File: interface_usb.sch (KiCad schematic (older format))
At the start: 0 parts

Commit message: Various components added
USB conn, general outputs, brake signal, touch sensor
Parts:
- added U?: CONN_USB, symbol CONN_USB
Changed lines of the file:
@@
 $Descr A4 11693 8268
 encoding utf-8
-Sheet 4 11
+Sheet 5 11
 Title ""
 Date "11 nov 2013"
@@
 Comment4 ""
 $EndDescr
+$Comp
+L CONN_USB U?
+U 1 1 52807223
+P 850 550
+F 0 "U?" H 850 550 60  0000 C CNN
+F 1 "CONN_USB" H 850 -100 60  0000 C CNN
+F 2 "" H 850 550 60  0000 C CNN
+F 3 "" H 850 550 60  0000 C CNN
+	1    850  550
+	1    0    0    -1
+$EndComp
 $EndSCHEMATC

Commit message: started fleshing out USB comm circuits
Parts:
- added C?: 22nF, ~, symbol C
- added C?: Cap Nominal, ~, symbol C
- added C?: Cap Steadystate, ~, symbol C
- added R?: 10K, ~, symbol R
- added R?: Nominal, ~, symbol R
- added U?: CP2110, symbol CP2110
- added U?: ESDR0502N, symbol ESDR0502N
- added U?: AT42QT1011, symbol AT42QT1011
- added U?: TOUCHPAD, symbol TOUCHPAD
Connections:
- net labels added: +3.3V, DGND, TOUCH_1
- wire segments 0 -> 34
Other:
- moved on the sheet: U?
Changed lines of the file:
@@
 Sheet 8 14
 Title ""
-Date "23 nov 2013"
+Date "24 nov 2013"
 Rev ""
 Comp ""
@@
 L CONN_USB U?
 U 1 1 52807223
-P 850 550
-F 0 "U?" H 850 550 60  0000 C CNN
-F 1 "CONN_USB" H 850 -100 60  0000 C CNN
-F 2 "" H 850 550 60  0000 C CNN
-F 3 "" H 850 550 60  0000 C CNN
-	1    850  550
-	1    0    0    -1
-$EndComp
+P 1650 2800
+F 0 "U?" H 1650 2800 60  0000 C CNN
+F 1 "CONN_USB" H 1650 2150 60  0000 C CNN
+F 2 "" H 1650 2800 60  0000 C CNN
+F 3 "" H 1650 2800 60  0000 C CNN
+	1    1650 2800
+	1    0    0    -1
+$EndComp
+$Comp
+L CP2110 U?
+U 1 1 5291A63B
+P 4250 2400
+F 0 "U?" H 4250 2400 60  0000 C CNN
+F 1 "CP2110" H 4250 700 60  0000 C CNN
+F 2 "" H 4250 2400 60  0000 C CNN
+F 3 "" H 4250 2400 60  0000 C CNN
+	1    4250 2400
+	1    0    0    -1
+$EndComp
+$Comp
+L ESDR0502N U?
+U 1 1 529256B4
+P 2700 2750
+F 0 "U?" H 2700 2750 60  0000 C CNN
+F 1 "ESDR0502N" H 2700 2050 60  0000 C CNN
+F 2 "" H 2700 2750 60  0000 C CNN
+F 3 "" H 2700 2750 60  0000 C CNN
+	1    2700 2750
+	1    0    0    -1
+$EndComp
+$Comp
+L AT42QT1011 U?
+U 1 1 52925A52
+P 3400 5700
+F 0 "U?" H 3400 5700 60  0000 C CNN
+F 1 "AT42QT1011" H 3400 4900 60  0000 C CNN
+F 2 "" H 3400 5700 60  0000 C CNN
+F 3 "" H 3400 5700 60  0000 C CNN
+	1    3400 5700
+	1    0    0    -1
+$EndComp
+$Comp
+L +3.3V #PWR?
+U 1 1 52925A58
+P 2450 4050
+F 0 "#PWR?" H 2450 4010 30  0001 C CNN
+F 1 "+3.3V" H 2450 4160 30  0000 C CNN
+F 2 "" H 2450 4050 60  0000 C CNN
+F 3 "" H 2450 4050 60  0000 C CNN
+	1    2450 4050
+	1    0    0    -1
+$EndComp
+$Comp
+L DGND #PWR?
+U 1 1 52925A5E
+P 2050 3400
+F 0 "#PWR?" H 2050 3400 40  0001 C CNN
+F 1 "DGND" H 2050 3330 40  0000 C CNN
+F 2 "" H 2050 3400 60  0000 C CNN
+F 3 "" H 2050 3400 60  0000 C CNN
+	1    2050 3400
+	1    0    0    -1
+$EndComp
+$Comp
+L R R?
+U 1 1 52925A64
+P 2200 5800
+F 0 "R?" V 2280 5800 40  0000 C CNN
+F 1 "10K" V 2207 5801 40  0000 C CNN
+F 2 "~" V 2130 5800 30  0000 C CNN
+F 3 "~" H 2200 5800 30  0000 C CNN
+	1    2200 5800
+	0    -1   -1   0
+$EndComp
+$Comp
+L C C?
+U 1 1 52925A6A
+P 2500 6000
+F 0 "C?" H 2400 6100 40  0000 L CNN
+F 1 "22nF" H 2600 6000 40  0000 L CNN
+F 2 "~" H 2538 5850 30  0000 C CNN
+F 3 "~" H 2500 6000 60  0000 C CNN
+	1    2500 6000
+	-1   0    0    1
+$EndComp
+$Comp
+L TOUCHPAD U?
+U 1 1 52925A70
+P 1600 5800
+F 0 "U?" H 1600 5900 60  0000 C CNN
+F 1 "TOUCHPAD" H 1600 5800 60  0000 C CNN
+F 2 "" H 1600 5800 60  0000 C CNN
+F 3 "" H 1600 5800 60  0000 C CNN
+	1    1600 5800
+	1    0    0    -1
+$EndComp
+$Comp
+L C C?
+U 1 1 52925A88
+P 2200 6600
+F 0 "C?" H 2200 6700 40  0000 L CNN
+F 1 "Cap Nominal" H 1800 6500 40  0000 L CNN
+F 2 "~" H 2238 6450 30  0000 C CNN
+F 3 "~" H 2200 6600 60  0000 C CNN
+	1    2200 6600
+	1    0    0    -1
+$EndComp
+$Comp
+L +3.3V #PWR?
+U 1 1 52925A8E
+P 2200 6350
+F 0 "#PWR?" H 2200 6310 30  0001 C CNN
+F 1 "+3.3V" H 2200 6460 30  0000 C CNN
+F 2 "" H 2200 6350 60  0000 C CNN
+F 3 "" H 2200 6350 60  0000 C CNN
+	1    2200 6350
+	1    0    0    -1
+$EndComp
+$Comp
+L C C?
+U 1 1 52925A96
+P 4050 6000
+F 0 "C?" H 4050 6100 40  0000 L CNN
+F 1 "Cap Steadystate" H 4056 5915 40  0000 L CNN
+F 2 "~" H 4088 5850 30  0000 C CNN
+F 3 "~" H 4050 6000 60  0000 C CNN
+	1    4050 6000
+	1    0    0    -1
+$EndComp
+$Comp
+L DGND #PWR?
+U 1 1 52925A9E
+P 4050 6250
+F 0 "#PWR?" H 4050 6250 40  0001 C CNN
+F 1 "DGND" H 4050 6180 40  0000 C CNN
+F 2 "" H 4050 6250 60  0000 C CNN
+F 3 "" H 4050 6250 60  0000 C CNN
+	1    4050 6250
+	1    0    0    -1
+$EndComp
+Text HLabel 4200 5800 2    60   Output ~ 0
+TOUCH_1
+$Comp
+L R R?
+U 1 1 52925AA7
+P 2500 6550
+F 0 "R?" V 2580 6550 40  0000 C CNN
+F 1 "Nominal" V 2507 6551 40  0000 C CNN
+F 2 "~" V 2430 6550 30  0000 C CNN
+F 3 "~" H 2500 6550 30  0000 C CNN
+	1    2500 6550
+	1    0    0    -1
+$EndComp
+Wire Wire Line
+	1950 5800 1900 5800
+Wire Wire Line
+	2450 5800 2500 5800
+Wire Wire Line
+	2500 5800 2650 5800
+Wire Wire Line
+	2650 5800 2650 5950
+Wire Wire Line
+	2650 5950 2800 5950
+Wire Wire Line
+	2500 6200 2650 6200
+Wire Wire Line
+	2650 6200 2650 6050
+Wire Wire Line
+	2650 6050 2800 6050
+Connection ~ 2500 5800
+Wire Wire Line
+	2800 5650 2800 5800
+Wire Wire Line
+	2800 6350 2800 6800
+Wire Wire Line
+	2800 6800 2800 6850
+Wire Wire Line
+	2700 6300 2700 6200
+Wire Wire Line
+	2700 6200 2800 6200
+Connection ~ 2800 6800
+Wire Wire Line
+	2700 6300 2500 6300
+Wire Wire Line
+	2200 6800 2500 6800
+Wire Wire Line
+	2500 6800 2800 6800
+Wire Wire Line
+	2200 6350 2200 6400
+Connection ~ 2500 6800
+Wire Wire Line
+	4000 5800 4050 5800
+Wire Wire Line
+	4050 5800 4200 5800
+Wire Wire Line
+	4050 6200 4050 6250
+Connection ~ 4050 5800
+Wire Wire Line
+	2300 3050 2300 2800
+Wire Wire Line
+	2300 2800 3100 2800
+Wire Wire Line
+	3100 2800 3100 3050
+Wire Wire Line
+	2300 3150 2300 3550
+Wire Wire Line
+	2300 3550 3100 3550
+Wire Wire Line
+	3100 3550 3100 3150
+Wire Wire Line
+	2000 2950 2100 2950
+Wire Wire Line
+	2000 3350 2050 3350
+Wire Wire Line
+	2050 3350 2100 3350
+Wire Wire Line
+	2050 3350 2050 3400
+Connection ~ 2050 3350
+Wire Wire Line
+	3100 3050 3400 3050
+Wire Wire Line
+	3100 3150 3400 3150
+Wire Wire Line
+	2000 3050 2300 3050
+Wire Wire Line
+	2000 3150 2300 3150
 $EndSCHEMATC

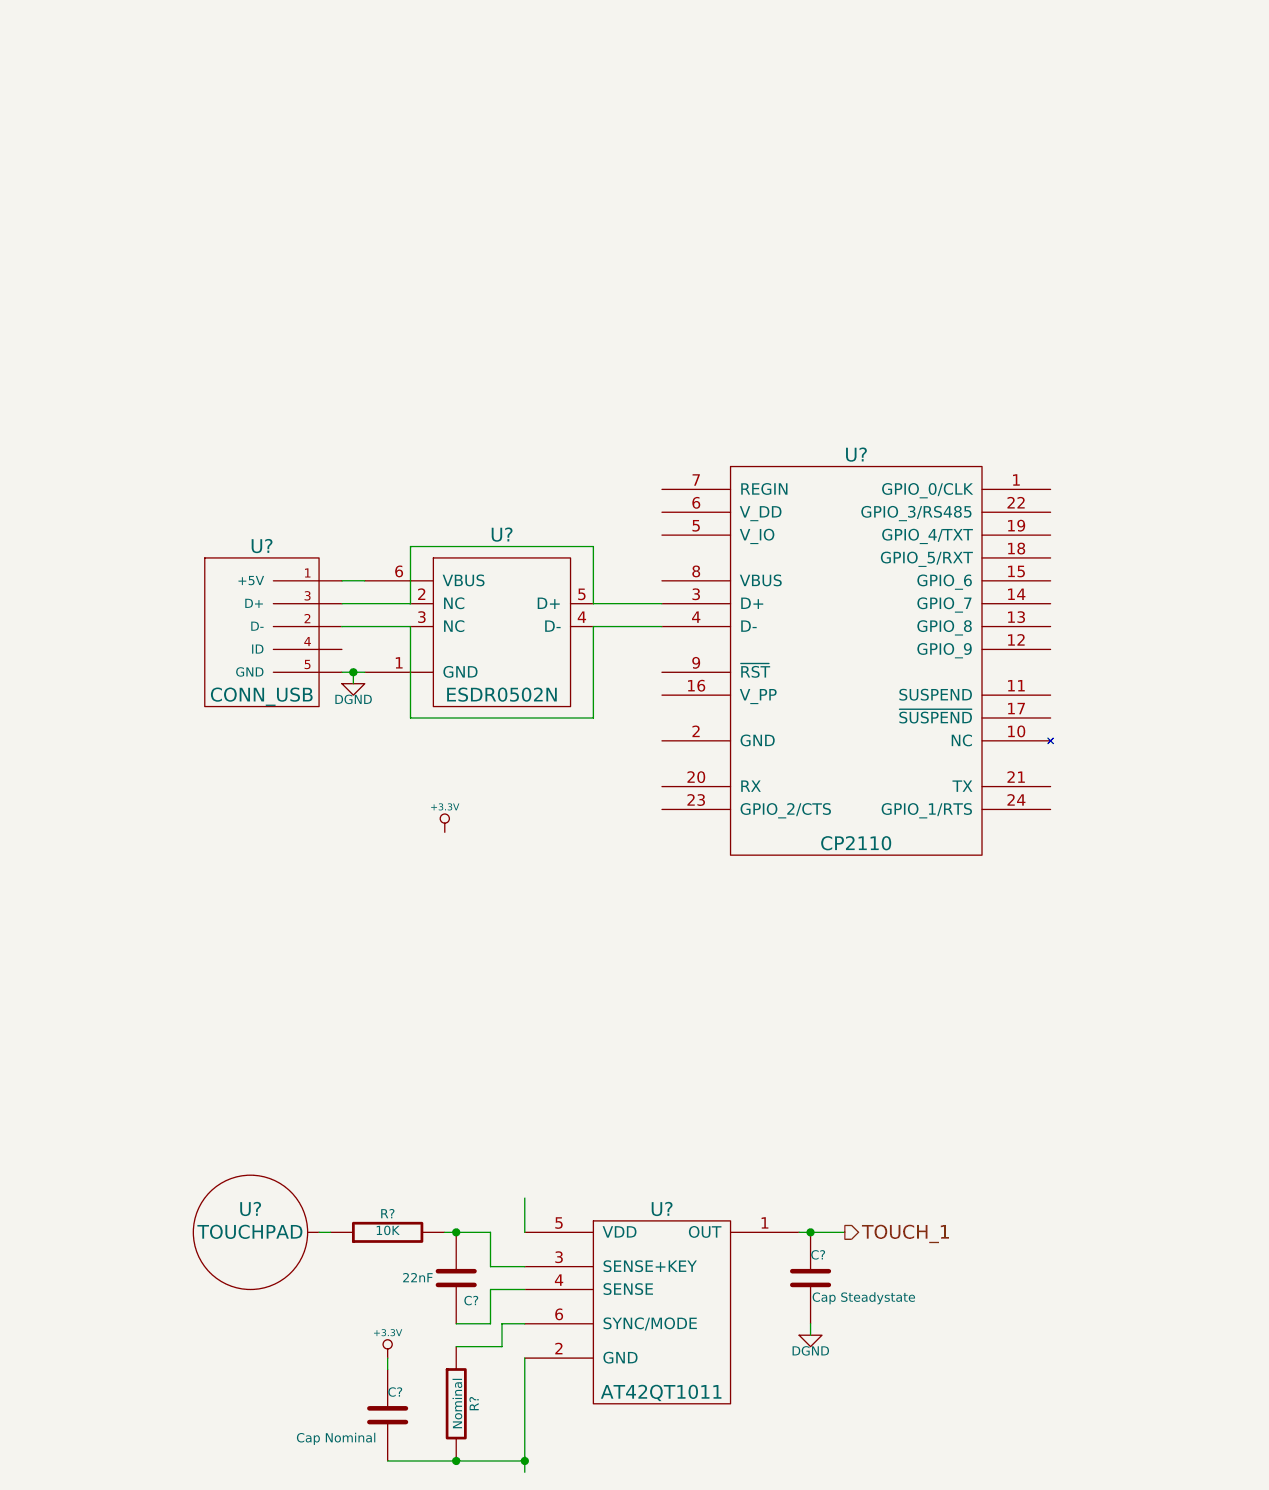
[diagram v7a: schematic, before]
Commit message: completed USB comm circuits
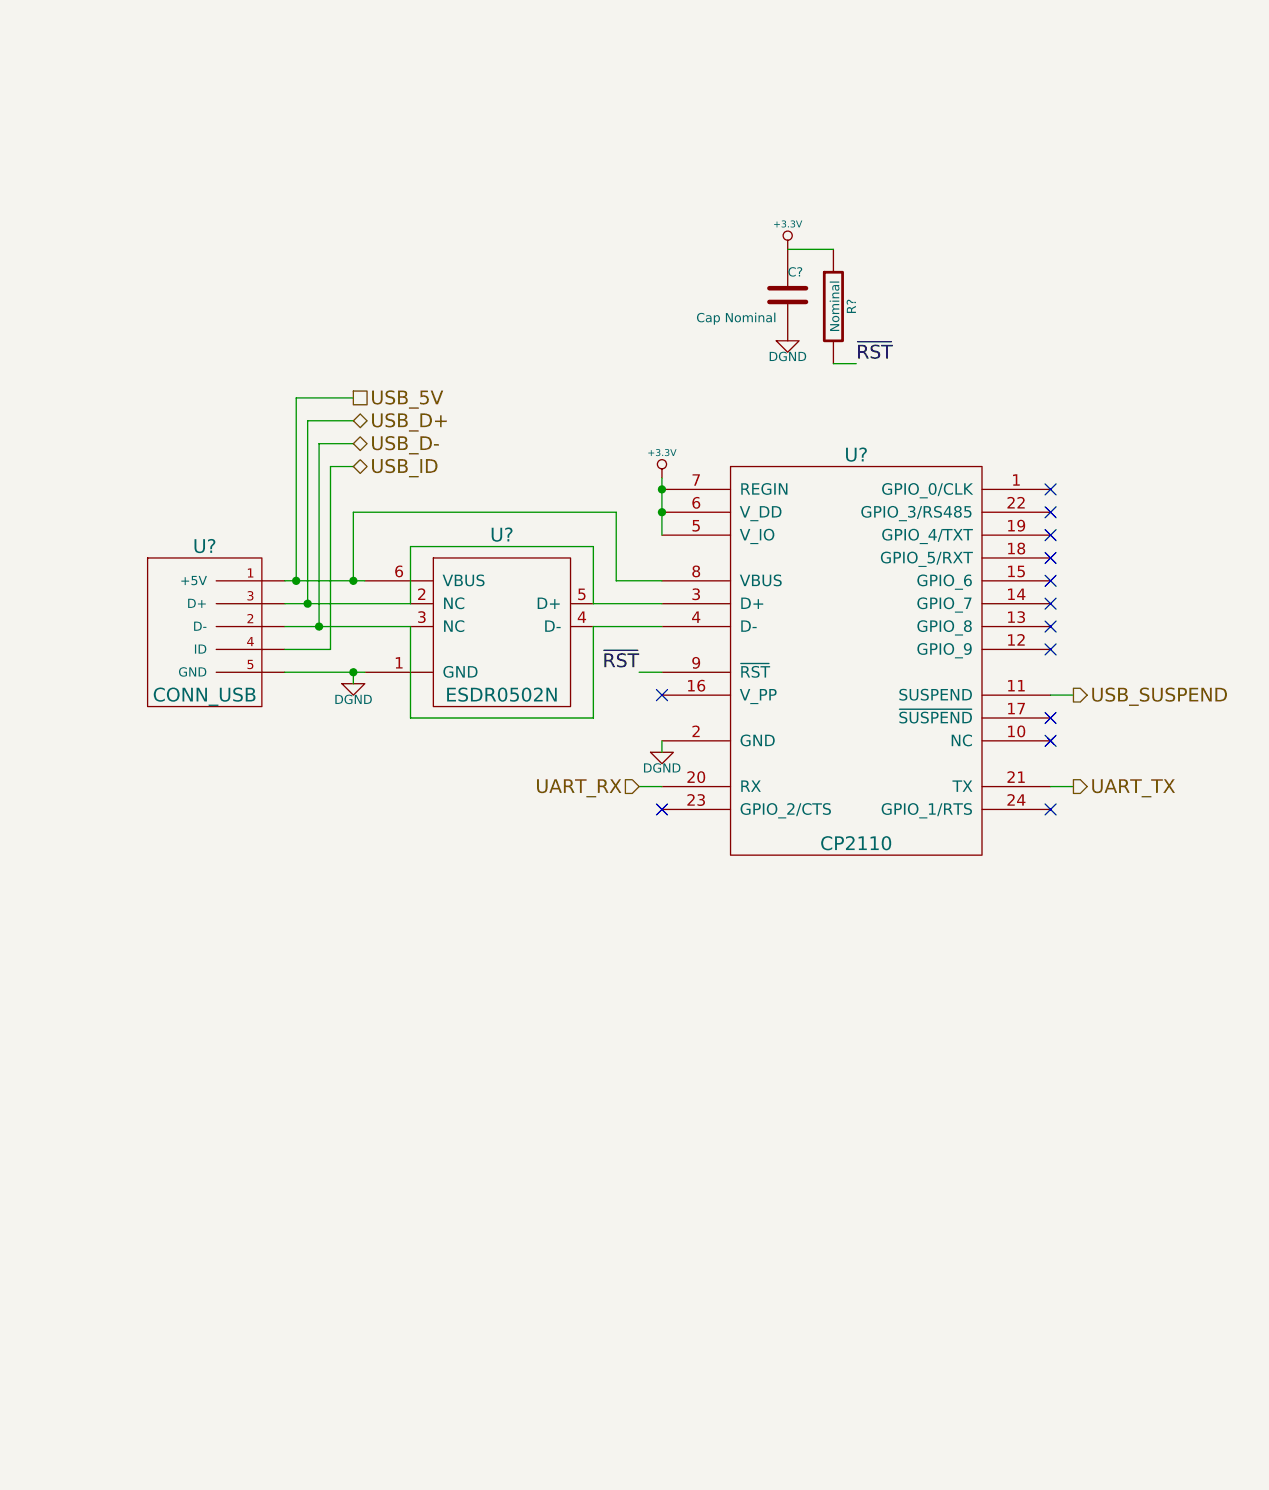
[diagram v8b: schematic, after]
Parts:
- removed C?: 22nF, ~, symbol C
- removed C?: Cap Nominal, ~, symbol C
- removed C?: Cap Steadystate, ~, symbol C
- removed R?: 10K, ~, symbol R
- removed R?: Nominal, ~, symbol R
- removed U?: AT42QT1011, symbol AT42QT1011
- removed U?: TOUCHPAD, symbol TOUCHPAD
- added C?: Cap Nominal, ~, symbol C
- added R?: Nominal, ~, symbol R
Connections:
- net labels added: UART_RX, UART_TX, USB_5V, USB_D+, USB_D-, USB_ID, USB_SUSPEND, ~RST
- net labels removed: TOUCH_1
- wire segments 34 -> 41
- no-connect marks 0 -> 13
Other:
- moved on the sheet: U?
